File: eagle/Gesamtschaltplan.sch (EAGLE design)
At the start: 173 parts, among them IC1 LM350T, IC2 LM350T, IC3 ATMEGA328P, IC4 7818TV, IC5 DCDC-WANDLER, Q1 BC550C, Q10 AUIRF8409, Q11 AUIRF8409, Q12 AUIRF8409, Q13 AUIRF8409, Q14 AUIRF8409, Q15 AUIRF8409, Q16 AUIRF8409, Q17 AUIRF8409, Q18 AUIRF8409, Q19 AUIRF8409, Q2 IRF1234, Q20 AUIRF8409, Q21 AUIRF8409, Q3 IRF1234, Q4 IRF1234, Q5 IRF1234, Q6 IRF1234, Q7 IRF1234, Q8 AUIRF8409, Q9 AUIRF8409, X1 MKDSN1,5/3-5,08, X2 MKDSN1,5/2-5,08, X3 MKDSN1,5/2-5,08, X4 MKDSN1,5/2-5,08, X5 MKDSN1,5/2-5,08, X6 MKDSN1,5/2-5,08, X7 1751251

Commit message: Added forgotten Pull-Down resistors. Lots of new code for executing mosfets
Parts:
- added R28: 220, resistor:R-EU_R1206
- added R39, R48: 10R, rcl:R-EU_R1206
- C1, C2: value 1n -> 1000µ; device rcl:C-EUC0603K -> rcl:CPOL-EUE5-13
- C10, C11: value 22pF -> 100 µF; device resistor:C-EUC0603K -> rcl:CPOL-EUE2.5-7
- C12: value 100 nF -> 100 µF; device resistor:C-EUC0603 -> rcl:CPOL-EUE2.5-7
- C14: value 100 nF -> 1000µ; device resistor:C-EUC0603 -> rcl:CPOL-EUE3.5-8
- C15, C16: value 100 µF -> 100nF; device rcl:CPOL-EUE2.5-7 -> rcl:C-EUC0805
- C18, C20: value 1000µ -> 100nF; device rcl:CPOL-EUE5-13 -> rcl:C-EUC0805
- C21: value 1000µ -> 100 nF; device rcl:CPOL-EUE5-13 -> resistor:C-EUC0603
- C22, C23: value 100nF -> 100 nF; device rcl:C-EUC0805 -> resistor:C-EUC0603
- C24: value 1000µ -> 100 nF; device rcl:CPOL-EUE3.5-8 -> resistor:C-EUC0603
- C25, C26: value 100nF -> 22pF; device rcl:C-EUC0805 -> resistor:C-EUC0603K
- C27: value 47000 uF -> 1n; device rcl:CPOL-EUE5-9VAXIAL -> rcl:C-EUC0603K
- C28, C29: value 100000uF -> 1n; device rcl:CPOL-EUE5-9VAXIAL -> rcl:C-EUC0603K
- C3: value 1µ -> 1000µ; device rcl:CPOL-EUE5-8.5 -> rcl:CPOL-EUE5-13
- C4: value 100 nF -> 47000 uF; device resistor:C-EUC0603 -> rcl:CPOL-EUE5-9VAXIAL
- C5: value 1µ -> 100000uF; device rcl:CPOL-EUE5-8.5 -> rcl:CPOL-EUE5-9VAXIAL
- C6: value 100 nF -> 100000uF; device resistor:C-EUC0603 -> rcl:CPOL-EUE5-9VAXIAL
- C7: value 1n -> 1µ; device rcl:C-EUC0603K -> rcl:CPOL-EUE5-8.5
- C8: value 100 µF -> 1µ; device rcl:CPOL-EUE2.5-7 -> rcl:CPOL-EUE5-8.5
- C9: value 100 µF -> 100 µF
- D1, D2, D4: value (none) -> 1N4004; device diode:ZENER-DIODESOT23 -> diode:1N4004
- D11, D12, D13: value 1N4004 -> 38V; device diode:1N4004 -> diode:ZENER-DIODEC1702-15
- D14, D15, D16: value 38V -> (none); device diode:ZENER-DIODEC1702-15 -> diode:ZENER-DIODESOT23
- F1: value (none) -> 500mA
- F2: value (none) -> 100mA
- IC1: value LM350T -> ATMEGA328P; device v-reg:LM317TS -> avr-6:MEGA48/88/168-PU
- IC3: value ATMEGA328P -> LM350T; device avr-6:MEGA48/88/168-PU -> v-reg:LM317TS
- JP1: device pinhead:PINHD-1X2 -> pinhead:PINHD-2X3
- JP12: device pinhead:PINHD-1X5 -> pinhead:PINHD-1X2
- JP2: device pinhead:PINHD-1X2 -> pinhead:PINHD-1X16
- JP3: device pinhead:PINHD-1X2 -> pinhead:PINHD-1X5
- JP4: device pinhead:PINHD-1X2 -> pinhead:PINHD-1X4
- JP7: device pinhead:PINHD-1X16 -> pinhead:PINHD-1X2
- JP8: device pinhead:PINHD-2X3 -> pinhead:PINHD-1X2
- JP9: device pinhead:PINHD-1X4 -> pinhead:PINHD-1X2
- Q1: value BC550C -> AUIRF8409; device transistor-npn:BC550C -> transistor-power:PMOSFET_NTO220BH
- Q2, Q3: value IRF1234 -> AUIRF8409
- Q21: value AUIRF8409 -> BC550C; device transistor-power:PMOSFET_NTO220BH -> transistor-npn:BC550C
- Q8, Q9: value AUIRF8409 -> IRF1234
- R1: value 150R -> 10k; device rcl:R-EU_R1206 -> pot:TRIM_EU-PT10
- R11: value 10k -> 5R6 50W; device pot:TRIM_EU-PT10 -> rcl:R-EU_R1206
- R12, R13, R14: value 150 -> 20R 1W; device resistor:R-EU_0411/15 -> rcl:R-EU_R1206
- R15: value 560 -> 20R 1W; device resistor:R-EU_R1206 -> rcl:R-EU_R1206
- R16: value 3k9 -> 20R 1W; device resistor:R-EU_R1206 -> rcl:R-EU_R1206
- R17, R20: value 180R -> 20R 1W
- R18, R21: value (none) -> 20R 1W; device pot:TRIM_EU-PT10 -> rcl:R-EU_R1206
- R19: value 10R -> 20R 1W
- R2: value 1k -> (none); device resistor:R-EU_R1206 -> pot:TRIM_EU-PT10
- R22: value 50k -> 150R
- R23: value 10R -> 150R
- R24, R25: value 10R -> 180R
- R26: value 10R -> 1k; device rcl:R-EU_R1206 -> resistor:R-EU_R1206
- R27: value 10R -> 33k; device rcl:R-EU_R1206 -> resistor:R-EU_R1206
- R29: value (none) -> 560; device pot:TRIM_EU-PT10 -> resistor:R-EU_R1206
- R3: value 33k -> (none); device resistor:R-EU_R1206 -> pot:TRIM_EU-PT10
- R30: value (none) -> 3k9; device pot:TRIM_EU-PT10 -> resistor:R-EU_R1206
- R31, R33: value 10R -> 560; device rcl:R-EU_R1206 -> resistor:R-EU_R1206
- R32, R34: value 10R -> 3k9; device rcl:R-EU_R1206 -> resistor:R-EU_R1206
- R36: value 10R -> 50k
- R38, R47: value 50k -> 10R
- R4: value 220 -> 5k; device resistor:R-EU_R1206 -> pot:TRIM_EU-PT10
- R40, R41, R42, R43, R44, R45, R46: value 10 -> 10R
- R49: value (none) -> 50k; device pot:TRIM_EU-PT10 -> rcl:R-EU_R1206
- R5: value 150R -> 5k; device rcl:R-EU_R1206 -> pot:TRIM_EU-PT10
- R50, R51, R52, R53, R54, R55, R56: value 20R 1W -> 10R
- R57: value 20R 1W -> 50k
- R58: value 20R 1W -> 2k
- R59: value 20R 1W -> 10k; device rcl:R-EU_R1206 -> resistor:R-EU_R1206
- R6: value 560 -> 10k; device resistor:R-EU_R1206 -> pot:TRIM_EU-PT10
- R60: value 5R6 50W -> 10k; device rcl:R-EU_R1206 -> resistor:R-EU_R1206
- R61: value 2k -> 10k; device rcl:R-EU_R1206 -> resistor:R-EU_R1206
- R7, R9: value 3k9 -> 150; device resistor:R-EU_R1206 -> resistor:R-EU_0411/15
- R8: value 560 -> 150; device resistor:R-EU_R1206 -> resistor:R-EU_0411/15
- U$2: value ABRACON_ABM3_CRYSTALABM03_HC49 -> GLEICHRICHTER; device Ava:ABRACON_ABM3_CRYSTALABM03_HC49 -> Gleichrichter:GLEICHRICHTER
- U$3: value MCP1407MCP1407-DIL08 -> VOLTMETER; device 0liver:MCP1407MCP1407-DIL08 -> 0liver:VOLTMETER
- U$6: value GLEICHRICHTER -> MCP1407MCP1407-DIL08; device Gleichrichter:GLEICHRICHTER -> 0liver:MCP1407MCP1407-DIL08
- U$7: value VOLTMETER -> ABRACON_ABM3_CRYSTALABM03_HC49; device 0liver:VOLTMETER -> Ava:ABRACON_ABM3_CRYSTALABM03_HC49
- X1: value MKDSN1,5/3-5,08 -> MKDSN1,5/2-5,08; device con-phoenix-508:MKDSN1,5/3-5,08 -> con-phoenix-508:MKDSN1,5/2-5,08
- X6: value MKDSN1,5/2-5,08 -> MKDSN1,5/3-5,08; device con-phoenix-508:MKDSN1,5/2-5,08 -> con-phoenix-508:MKDSN1,5/3-5,08
- renumbered JP18 to JP17
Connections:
- net C1V: now also D4.A, D6.A, JP4.3, JP6.1, R12.1, R13.1, R14.1, R15.1, R16.1, R32.1, U$3.P$1; no longer D7.A, D9.A, JP1.1, JP5.3, R50.1, R51.1, R52.1, R53.1, R54.1, R9.1, U$7.P$1
- net C1V1: now also R17.1, R18.1, R19.1, R20.1, R21.1; no longer R55.1, R56.1, R57.1, R58.1, R59.1
- net C2V: now also C4.+, D12.C, D5.C, D9.A, JP4.1, Q8.D, Q9.D, R30.1; no longer C27.+, D12.A, D15.C, D8.C, JP5.1, Q2.D, Q3.D, R7.1
- net DATA0: now also IC1.PD2(INT0/PCINT18), JP2.11; no longer IC3.PD2(INT0/PCINT18), JP7.11
- net DATA1: now also IC1.PD3(INT1/OC2B/PCINT19), JP2.12; no longer IC3.PD3(INT1/OC2B/PCINT19), JP7.12
- net DATA2: now also IC1.PD4(T0/XCK/PCINT20), JP2.13; no longer IC3.PD4(T0/XCK/PCINT20), JP7.13
- net DATA3: now also IC1.PD5(T1/OC0B/PCINT21), JP2.14; no longer IC3.PD5(T1/OC0B/PCINT21), JP7.14
- net FET1: now also JP3.5, U$6.IN; no longer JP12.5, U$5.IN
- net FET2: now also IC1.PD6(AIN0/OC0A/PCINT22), JP3.4, JP5.2, R60.1, U$5.IN; no longer IC3.PD6(AIN0/OC0A/PCINT22), JP12.4, JP9.2, U$4.IN
- net FET3: now also IC1.PD7(AIN1/PCINT23), JP3.3, JP5.3, R61.1, U$4.IN; no longer IC3.PD7(AIN1/PCINT23), JP12.3, JP9.3, U$3.IN
- net GND: now also C1.-, C14.-, C15.2, C16.2, C18.2, C2.-, C20.2, C21.2, C24.2, C27.1, C28.1, C29.1, C4.-, C5.-, C6.-, C7.-, C8.-, D11.A, D12.A, D13.A, IC1.AGND, IC1.GND@1, JP1.6, JP10.2, JP11.1, JP12.2, JP2.16, JP2.5, JP4.2, JP5.4, JP8.1, R1.E, R11.2, R2.E, R2.S, R27.2, R29.2, R3.E, R3.S, R31.2, R33.2, R36.2, R49.2, R57.2, R59.2, R61.2, R7.1, R8.1, R9.1, U$2.-, U$3.P$2, U$4.GND, U$6.GND, X2-1.KL, X5-1.KL; no longer C1.1, C10.2, C11.2, C12.2, C13.-, C14.2, C18.-, C2.1, C20.-, C21.-, C22.2, C24.-, C27.-, C28.-, C29.-, C4.2, C7.1, D1.A, D2.A, D4.A, IC3.AGND, IC3.GND@1, JP1.2, JP10.1, JP11.2, JP12.1, JP5.2, JP7.16, JP7.5, JP8.6, JP9.4, R11.E, R12.1, R13.1, R14.1, R15.2, R18.E, R18.S, R21.E, R21.S, R22.2, R3.2, R38.2, R47.2, R6.2, R8.2, U$3.GND, U$5.GND, U$6.-, U$7.P$2, X4-1.KL, X6-1.KL
- net GND1: now also C13.-, C22.2, U$5.GND; no longer C5.-, C6.2, U$4.GND
- net LED: now also IC1.PB0(ICP1/CLKO/PCINT0), R28.1; no longer IC3.PB0(ICP1/CLKO/PCINT0), R4.1
- net MISO: now also IC1.PB4(MISO/PCINT4), JP1.1, JP5.1, R59.1; no longer IC3.PB4(MISO/PCINT4), JP8.1, JP9.1
- net MOSI: now also IC1.PB3(MOSI/OC2A/PCINT3), JP1.4; no longer IC3.PB3(MOSI/OC2A/PCINT3), JP8.4
- net N$1: now also JP12.1, R23.1; no longer JP11.1, R5.1
- net N$10: now also IC1.PC0(ADC0/PCINT8), JP7.2; no longer IC3.PC0(ADC0/PCINT8), JP2.2
- net N$12: now also IC1.PC1(ADC1/PCINT9), JP8.2; no longer IC3.PC1(ADC1/PCINT9), JP3.2
- net N$13: now also JP9.2, R6.E; no longer JP4.2, R49.E
- net N$14: now also D10.A, R58.2; no longer D13.A, R61.2
- net N$16: now also C10.-, C11.-, C12.-, R7.2, R8.2, R9.2; no longer C15.-, C16.-, C8.-, R12.2, R13.2, R14.2
- net N$18: now also C28.2, D15.C, IC1.PC2(ADC2/PCINT10), R33.1, R34.2; no longer C2.2, D2.C, IC3.PC2(ADC2/PCINT10), R15.1, R16.2
- net N$2: now also IC1.PC5(ADC5/SCLPCINT13), R23.2; no longer IC3.PC5(ADC5/SCLPCINT13), R5.2
- net N$20: now also IC2.ADJ, R25.1, R4.A; no longer IC1.ADJ, R20.1, R29.A
- net N$21: now also D5.A; no longer D8.A
- net N$22: now also JP9.1, Q21.E, R6.A, R6.S; no longer JP4.1, Q1.E, R49.A, R49.S
- net N$23: now also R2.A, R5.E, R5.S; no longer R18.A, R30.E, R30.S
- net N$24: now also X1-2.KL; no longer X2-2.KL
- net N$25: now also X1-1.KL; no longer X2-1.KL
- net N$26: now also IC1.PB1(OC1A/PCINT1), R22.2; no longer IC3.PB1(OC1A/PCINT1), R1.2
- net N$27: now also C26.1, IC1.PB7(XTAL2/TOSC2/PCINT7), U$7.2; no longer C11.1, IC3.PB7(XTAL2/TOSC2/PCINT7), U$2.2
- net N$28: now also C25.1, IC1.PB6(XTAL1/TOSC1/PCINT6), U$7.1; no longer C10.1, IC3.PB6(XTAL1/TOSC1/PCINT6), U$2.1
- net N$29: now also R3.A, R4.E, R4.S; no longer R21.A, R29.E, R29.S
- net N$3: now also C10.+, C11.+, C12.+, C21.1, C22.1, C24.1, C7.+, JP3.2, R58.1, U$6.VDD; no longer C14.1, C15.+, C16.+, C3.+, C4.1, C5.+, C6.1, JP12.2, R61.1, U$3.VDD
- net N$30: now also R11.1; no longer R60.1
- net N$35: now also D9.C; no longer D12.C
- net N$36: now also C1.+, C15.1, C16.1, C2.+, C3.+, D1.C, D2.C, IC3.IN; no longer C18.+, C19.1, C20.+, C21.+, C22.1, D5.C, D6.C, IC1.IN
- net N$37: now also C18.1, D3.A; no longer C23.1, D6.A
- net N$38: now also C14.+, C19.1, U$2.+; no longer C24.+, C25.1, U$6.+
- net N$39: now also X4-1.KL; no longer X5-1.KL
- net N$4: now also Q21.B, R26.2; no longer Q1.B, R2.2
- net N$40: now also X4-2.KL; no longer X5-2.KL
- net N$41: now also U$2.AC2; no longer U$6.AC2
- net N$42: now also U$2.AC1; no longer U$6.AC1
- net N$43: now also Q7.G, R35.2; no longer Q5.G, R19.2
- net N$44: now also Q4.G, R37.2; no longer Q2.G, R23.2
- net N$45: now also Q5.G, R38.2; no longer Q3.G, R24.2
- net N$47: now also JP2.15, R28.2; no longer JP7.15, R4.2
- net N$5: now also C29.2, D16.C, IC1.PC4(ADC4/SDA/PCINT12), R31.1, R32.2; no longer C7.2, D4.C, IC3.PC4(ADC4/SDA/PCINT12), R8.1, R9.2
- net N$52: now also Q6.G, R39.2; no longer Q4.G, R25.2
- net N$53: now also Q8.G, R40.2; no longer Q6.G, R26.2
- net N$54: now also Q9.G, R41.2; no longer Q7.G, R27.2
- net N$55: now also R35.1, R36.1, R37.1, R38.1, R39.1, R40.1, R41.1, U$6.OUT, X6-1.KL; no longer R19.1, R22.1, R23.1, R24.1, R25.1, R26.1, R27.1, U$5.OUT, X1-1.KL
- net N$56: now also R17.2, R18.2, R19.2, R20.2, R21.2; no longer R55.2, R56.2, R57.2, R58.2, R59.2
- net N$57: now also D1.A, IC2.OUT, R12.2, R13.2, R14.2, R15.2, R16.2, R25.2, X2-2.KL; no longer D3.A, IC1.OUT, R20.2, R50.2, R51.2, R52.2, R53.2, R54.2, X3-2.KL
- net N$59: now also IC3.ADJ, R24.1; no longer IC2.ADJ, R17.1
- net N$6: now also JP10.1, R22.1; no longer JP6.1, R1.1
- net N$60: now also D2.A, IC3.OUT, R24.2, X3-2.KL; no longer D5.A, IC2.OUT, R17.2, X4-2.KL
- net N$61: now also Q20.G, R42.2; no longer Q8.G, R31.2
- net N$62: now also Q10.G, R43.2; no longer Q9.G, R32.2
- net N$63: now also Q11.G, R44.2; no longer Q10.G, R33.2
- net N$64: now also Q12.G, R45.2; no longer Q11.G, R34.2
- net N$65: now also Q13.G, R46.2; no longer Q12.G, R35.2
- net N$66: now also Q14.G, R47.2; no longer Q13.G, R36.2
- net N$67: now also Q15.G, R48.2; no longer Q14.G, R37.2
- net N$68: now also R42.1, R43.1, R44.1, R45.1, R46.1, R47.1, R48.1, R49.1, U$5.OUT, X6-2.KL; no longer R31.1, R32.1, R33.1, R34.1, R35.1, R36.1, R37.1, R38.1, U$4.OUT, X1-2.KL
- net N$69: now also C6.+, D11.C, D6.C, D7.A, Q15.D, Q20.D; no longer C29.+, D10.A, D14.C, D9.C, Q8.D, Q9.D
- net N$7: now also C27.2, D14.C, IC1.PC3(ADC3/PCINT11), R29.1, R30.2; no longer C1.2, D1.C, IC3.PC3(ADC3/PCINT11), R6.1, R7.2
- net N$70: now also Q16.G, R50.2; no longer Q15.G, R40.2
- net N$71: now also Q17.G, R51.2; no longer Q16.G, R41.2
- net N$72: now also Q18.G, R52.2; no longer Q17.G, R42.2
- net N$73: now also Q19.G, R53.2; no longer Q18.G, R43.2
- net N$74: now also Q1.G, R54.2; no longer Q19.G, R44.2
- net N$75: now also Q2.G, R55.2; no longer Q20.G, R45.2
- net N$76: now also Q3.G, R56.2; no longer Q21.G, R46.2
- net N$77: now also R50.1, R51.1, R52.1, R53.1, R54.1, R55.1, R56.1, R57.1, U$4.OUT, X6-3.KL; no longer R40.1, R41.1, R42.1, R43.1, R44.1, R45.1, R46.1, R47.1, U$3.OUT, X1-3.KL
- net N$78: now also C5.+, D13.C, D4.C, D8.A, Q1.D, Q2.D, Q3.D; no longer C28.+, D11.A, D16.C, D7.C, Q15.D, Q20.D, Q21.D
- net N$8: now also JP2.3, R1.S; no longer JP7.3, R11.S
- net N$9: now also IC1.PB2(SS/OC1B/PCINT2), R26.1, R27.1; no longer IC3.PB2(SS/OC1B/PCINT2), R2.1, R3.1
- net RES: now also IC1.PC6(/RESET/PCINT14), JP1.5; no longer IC3.PC6(/RESET/PCINT14), JP8.5
- net RS: now also IC1.PD0(RXD/PCINT16), JP2.4; no longer IC3.PD0(RXD/PCINT16), JP7.4
- net RW: now also IC1.PD1(TXD/PCINT17), JP2.6; no longer IC3.PD1(TXD/PCINT17), JP7.6
- net SCK: now also IC1.PB5(SCK/PCINT5), JP1.3; no longer IC3.PB5(SCK/PCINT5), JP8.3
- net SENV: now also D10.C, JP4.4, Q1.S, R34.1, X5-2.KL; no longer D13.C, JP5.4, Q21.S, R16.1, X6-2.KL
- net VCC: now also C20.1, C23.1, IC1.AREF, IC1.AVCC, IC1.VCC@1, JP1.2, JP11.2, JP2.2, Q21.C, R1.A; no longer C12.1, C26.1, IC3.AREF, IC3.AVCC, IC3.VCC@1, JP10.2, JP7.2, JP8.2, Q1.C, R11.A
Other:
- moved on the sheet: C13, C17, C19, C22, C23, C25, C26, C3, C5, C8, C9, D10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

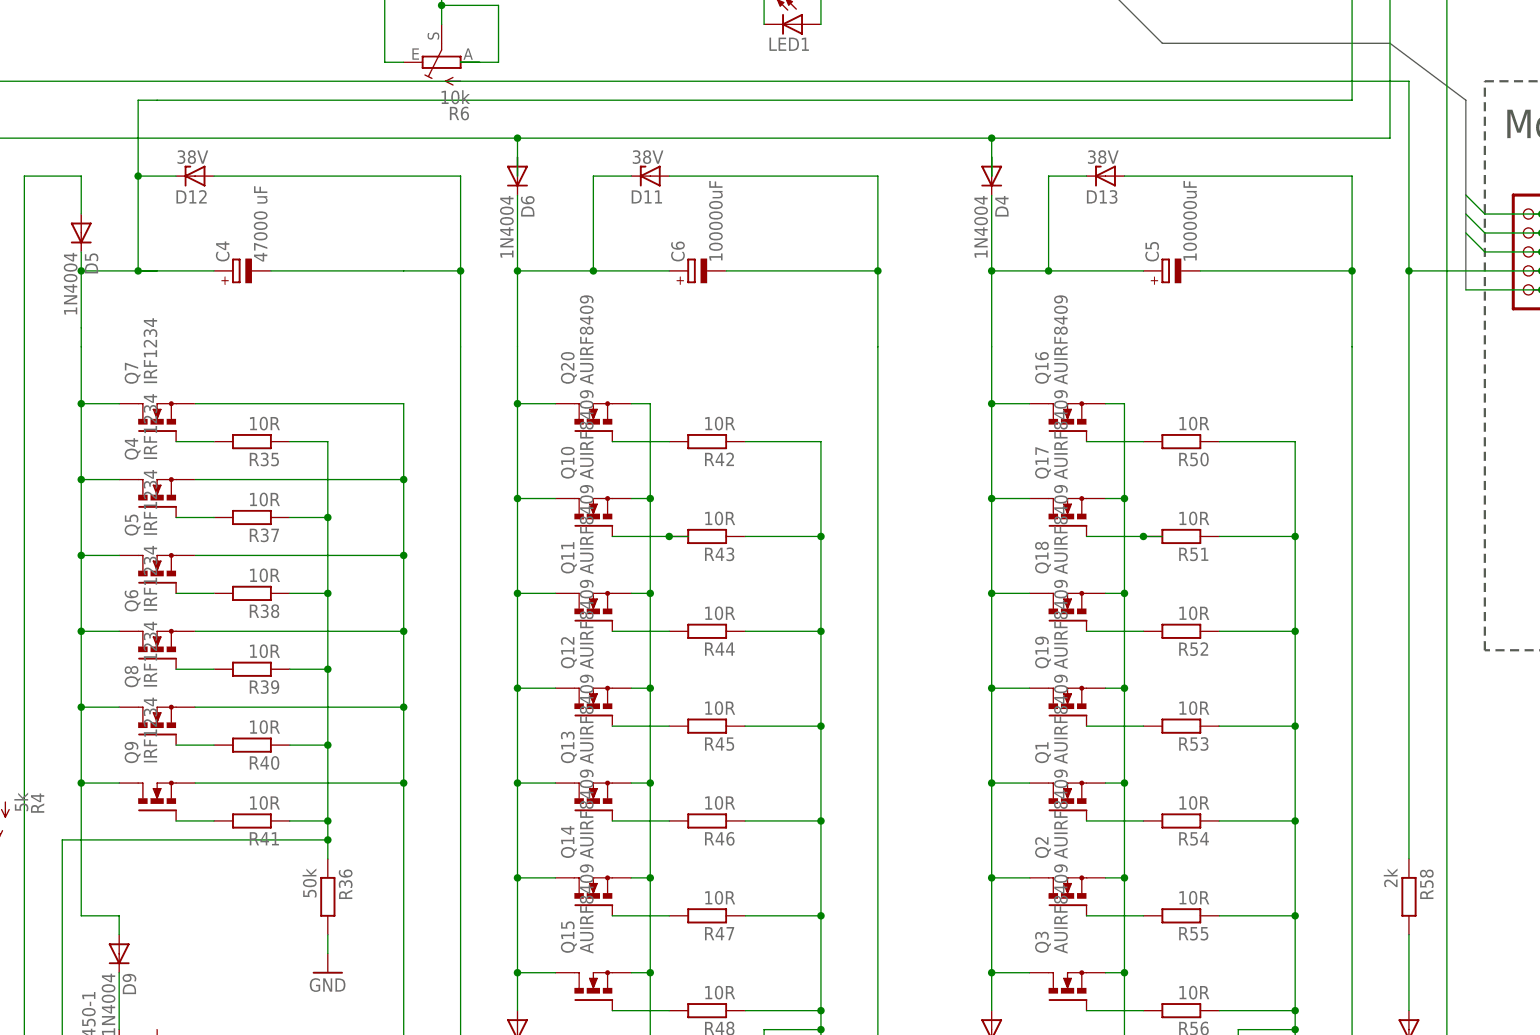
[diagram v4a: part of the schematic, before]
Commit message: added diode to driver power supply
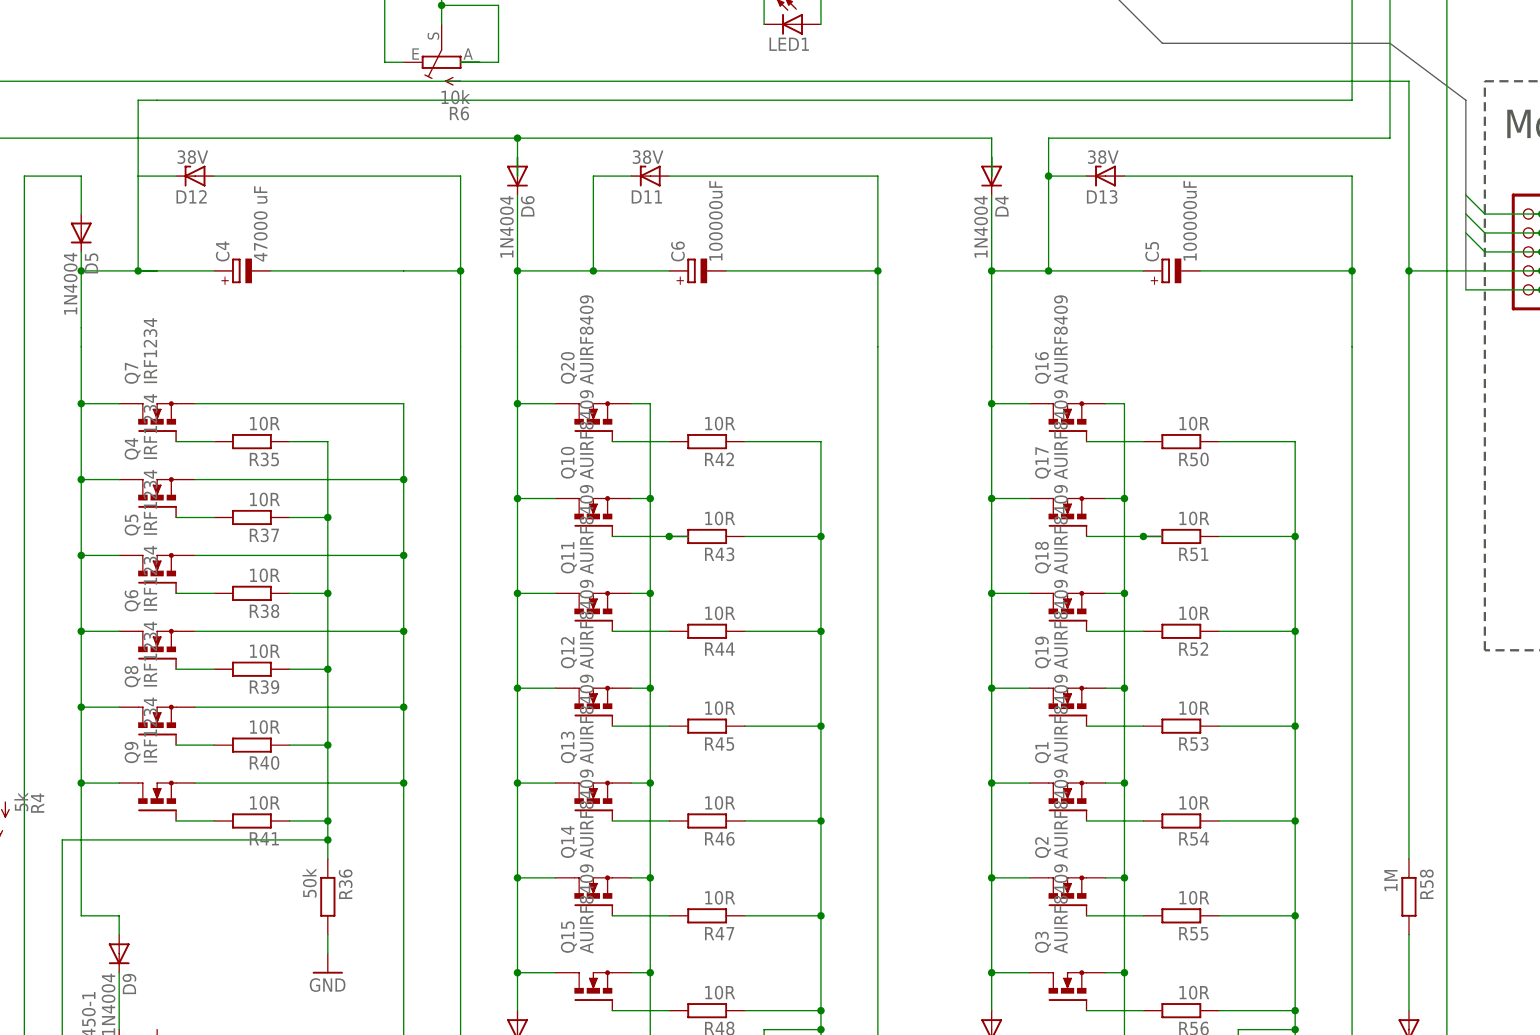
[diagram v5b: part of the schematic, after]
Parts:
- R58: value 2k -> 1M
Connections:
- removed net N$78: C5.+, D13.C, D4.C, D8.A, Q1.D, Q16.D, Q17.D, Q18.D, Q19.D, Q2.D, Q3.D
- new net N$15: C4.+, D12.C, D5.C, D9.A, Q4.D, Q5.D, Q6.D, Q7.D, Q8.D, Q9.D
- new net N$21: D4.A, D6.A, R12.1, R13.1, R14.1, R15.1, R16.1
- net C1V: now also C5.+, D13.C, D4.C, D8.A, Q1.D, Q16.D, Q17.D, Q18.D, Q19.D, Q2.D, Q3.D; no longer D4.A, D6.A, R12.1, R13.1, R14.1, R15.1, R16.1
- net C2V: no longer C4.+, D12.C, D5.C, D9.A, Q4.D, Q5.D, Q6.D, Q7.D, Q8.D, Q9.D
